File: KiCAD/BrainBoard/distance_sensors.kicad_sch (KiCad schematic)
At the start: 3 parts, among them J3 Conn_01x03_Socket, J4 Conn_01x03_Socket, J5 Conn_01x03_Socket

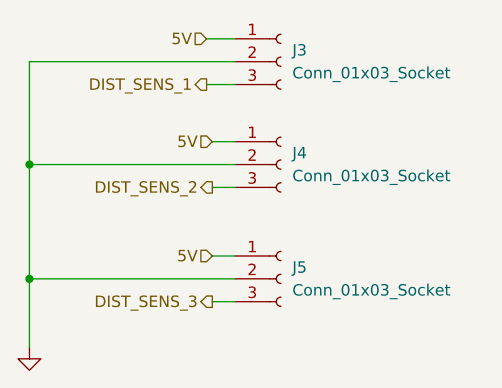
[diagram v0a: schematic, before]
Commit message: feat: add +5V line
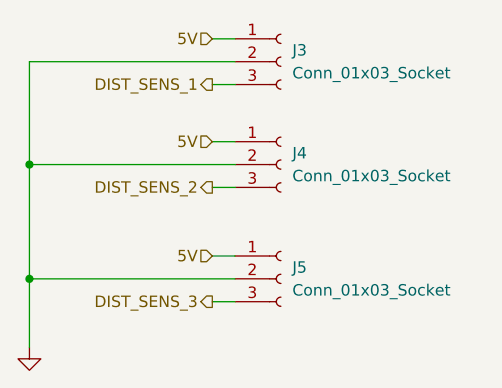
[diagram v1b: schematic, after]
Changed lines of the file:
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@@
 	(wire
 		(pts
-			(xy 133.985 80.01) (xy 137.16 80.01)
+			(xy 134.62 80.01) (xy 137.16 80.01)
 		)
 		(stroke
@@
 	(wire
 		(pts
-			(xy 133.985 85.09) (xy 137.16 85.09)
+			(xy 134.62 85.09) (xy 137.16 85.09)
 		)
 		(stroke
@@
 	(hierarchical_label "DIST_SENS_1"
 		(shape output)
-		(at 133.985 85.09 180)
+		(at 134.62 85.09 180)
 		(effects
 			(font
@@
 	(hierarchical_label "5V"
 		(shape input)
-		(at 133.985 80.01 180)
+		(at 134.62 80.01 180)
 		(effects
 			(font
